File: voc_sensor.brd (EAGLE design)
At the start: 28 x 32 mm, 14 parts, among them IC1 MP901, IC2 DS2438, IC3 7805DT, X1 MSTBV3

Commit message: changing some values: 5 Ohm resistor to 5.1 Ohm (5 Ohm is not broadly available) selected different type of TVS diode with essentially the same ratings
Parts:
- D1, D8: value SMA6F7.5A -> SMAJ7.5A-LF
- R1, R2, R4: value 5 -> 5.1
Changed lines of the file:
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@@
 <attribute name="NAME" x="15.105" y="1.867" size="1.016" layer="26" rot="MR0"/>
 </element>
-<element name="R1" library="rcl" package="R0402" value="5" x="8.6" y="6.8" smashed="yes" rot="MR180">
+<element name="R1" library="rcl" package="R0402" value="5.1" x="8.6" y="6.8" smashed="yes" rot="MR180">
 <attribute name="NAME" x="7.565" y="5.965" size="1.016" layer="26" rot="MR180"/>
 <attribute name="VALUE" x="7.965" y="8.705" size="1.016" layer="28" rot="MR180"/>
 </element>
-<element name="R2" library="rcl" package="R0402" value="5" x="6" y="25.4" smashed="yes" rot="MR180">
+<element name="R2" library="rcl" package="R0402" value="5.1" x="6" y="25.4" smashed="yes" rot="MR180">
 <attribute name="NAME" x="5.365" y="24.765" size="1.016" layer="26" rot="MR180"/>
 <attribute name="VALUE" x="5.365" y="27.105" size="1.016" layer="28" rot="MR180"/>
 </element>
-<element name="D8" library="diodes" package="DO214AC" value="SMA6F7.5A" x="3.8" y="6.8" smashed="yes" rot="MR0">
+<element name="D8" library="diodes" package="DO214AC" value="SMAJ7.5A-LF" x="3.8" y="6.8" smashed="yes" rot="MR0">
 <attribute name="NAME" x="4.64" y="3.886" size="1.016" layer="26" ratio="10" rot="MR0"/>
 </element>
@@
 <element name="IC3" library="linear" package="TO252" value="7805DT" x="20.4" y="25.8" smashed="yes" rot="MR270">
 <attribute name="NAME" x="25.59" y="27.14" size="1.016" layer="26" rot="MR270"/>
+<attribute name="MANF#" value="MC7805BDTG" x="20.4" y="25.8" size="1.778" layer="28" rot="MR270" display="off"/>
 </element>
 <element name="C1" library="rcl" package="C0805K" value="100n" x="12.6" y="28.6" smashed="yes" rot="MR270">
@@
 <attribute name="VALUE" x="9.9" y="31.8" size="1.016" layer="28" rot="MR270"/>
 </element>
-<element name="D1" library="diodes" package="DO214AC" value="SMA6F7.5A" x="2.4" y="27.4" smashed="yes" rot="MR270">
+<element name="D1" library="diodes" package="DO214AC" value="SMAJ7.5A-LF" x="2.4" y="27.4" smashed="yes" rot="MR270">
 <attribute name="NAME" x="1.114" y="28.24" size="1.016" layer="26" ratio="10" rot="MR270"/>
 </element>
-<element name="R4" library="rcl" package="R0402" value="5" x="5.8" y="29.4" smashed="yes" rot="MR180">
+<element name="R4" library="rcl" package="R0402" value="5.1" x="5.8" y="29.4" smashed="yes" rot="MR180">
 <attribute name="NAME" x="5.165" y="28.765" size="1.016" layer="26" rot="MR180"/>
 <attribute name="VALUE" x="5.365" y="31.105" size="1.016" layer="28" rot="MR180"/>

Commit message: changing load resistor to 100k as stated on the sensor packaging... already tried this and it works like a charm
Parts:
- R3: value 17k -> 100k
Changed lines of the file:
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@@
 <attribute name="NAME" x="1.496" y="14.945" size="1.016" layer="25" ratio="10" rot="R90"/>
 </element>
-<element name="R3" library="rcl" package="R0402" value="17k" x="15" y="10" smashed="yes" rot="MR0">
+<element name="R3" library="rcl" package="R0402" value="100k" x="15" y="10" smashed="yes" rot="MR0">
 <attribute name="NAME" x="19.035" y="9.435" size="1.016" layer="26" rot="MR0"/>
 <attribute name="VALUE" x="13.635" y="9.495" size="1.016" layer="28" rot="MR0"/>

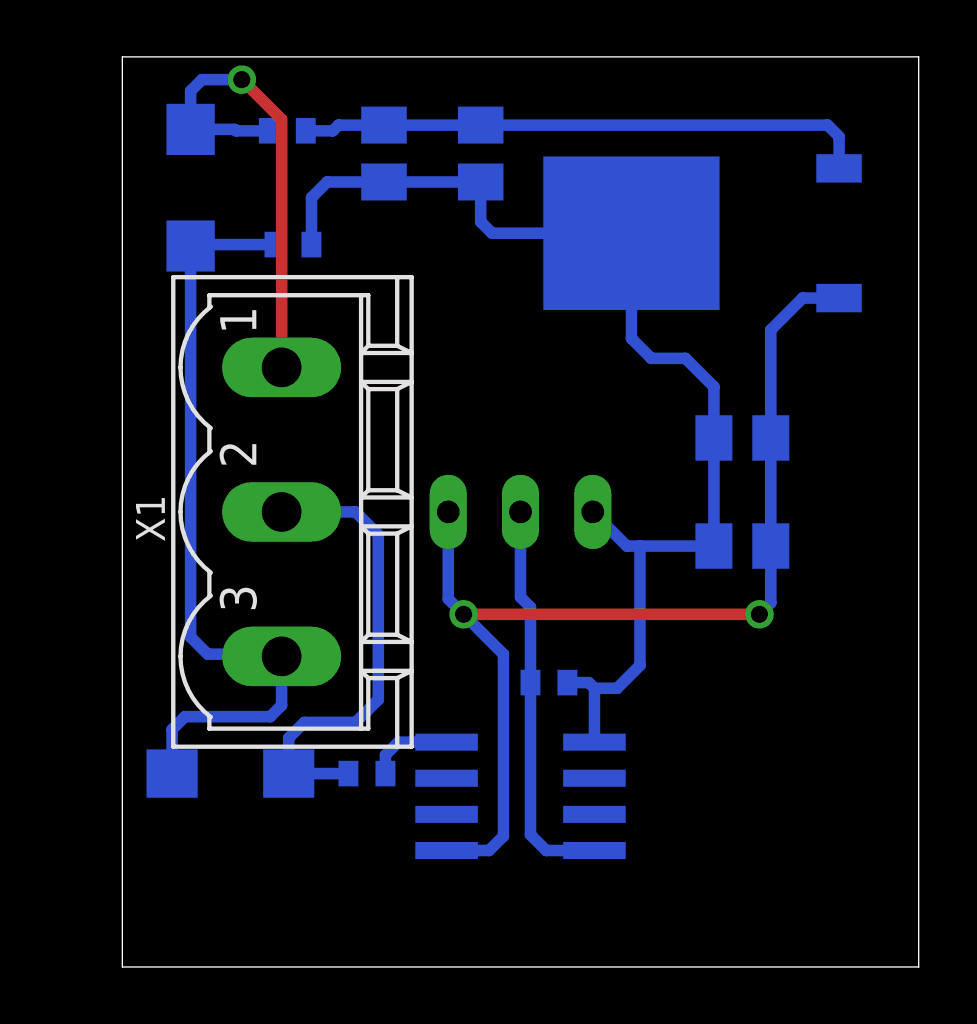
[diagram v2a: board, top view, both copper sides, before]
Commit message: replaced connector X1 to get a lower profile inside of the wall insert (resolves issue #2)
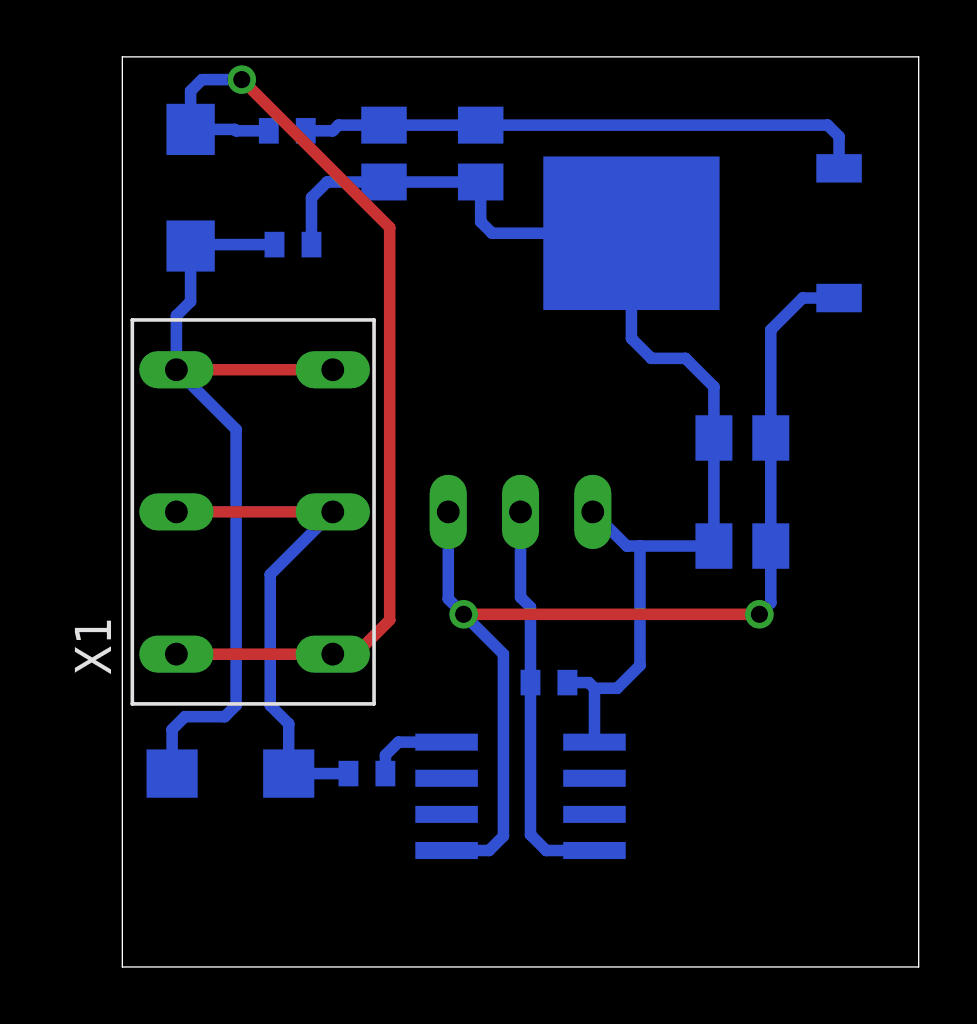
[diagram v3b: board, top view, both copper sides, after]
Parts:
- X1: value MSTBV3 -> SPRING_CLAMP_3_AST215; device con-phoenix-508:MSTBV3 -> connectors:AST215_3
- moved X1 1.00 mm to (4.60, 16.0), turned to 90 degrees
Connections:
- net N$10: now also X1.2A, X1.2B; no longer X1.2
- net N$4: now also X1.1A, X1.1B; no longer X1.1
- net N$5: now also X1.3A, X1.3B; no longer X1.3
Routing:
- net N$4: track 16.8 -> 35.2 mm
- net N$5: track 27.7 -> 29.8 mm
- net N$10: track 16.6 -> 18.0 mm
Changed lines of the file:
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@@
 <attribute name="NAME" x="4.64" y="3.886" size="1.016" layer="26" ratio="10" rot="MR0"/>
-</element>
-<element name="X1" library="con-phoenix-508" package="MSTBV3" value="MSTBV3" x="5.6" y="16" smashed="yes" rot="R270">
-<attribute name="OC_NEWARK" value="69R9846" x="-11.4" y="16" size="1.778" layer="27" rot="R270" display="off"/>
-<attribute name="MPN" value="MSTBV 2,5/3-GF-5.08" x="-11.4" y="16" size="1.778" layer="27" rot="R270" display="off"/>
-<attribute name="MF" value="" x="-11.4" y="16" size="1.778" layer="27" rot="R270" display="off"/>
-<attribute name="OC_FARNELL" value="1792793" x="-11.4" y="16" size="1.778" layer="27" rot="R270" display="off"/>
-<attribute name="NAME" x="1.496" y="14.945" size="1.016" layer="25" ratio="10" rot="R90"/>
 </element>
 <element name="R3" library="rcl" package="R0402" value="100k" x="15" y="10" smashed="yes" rot="MR0">
@@
 <attribute name="VALUE" x="5.365" y="31.105" size="1.016" layer="28" rot="MR180"/>
 </element>
+<element name="X1" library="connectors" package="AST215_3" value="SPRING_CLAMP_3_AST215" x="4.6" y="16" rot="R90"/>
 </elements>
 <signals>
@@
 <contactref element="R1" pad="1"/>
 <contactref element="D8" pad="C"/>
-<contactref element="X1" pad="2"/>
 <wire x1="5.85" y1="6.8" x2="7.95" y2="6.8" width="0.4064" layer="16"/>
-<wire x1="5.85" y1="6.8" x2="5.85" y2="8.05" width="0.4064" layer="16"/>
-<wire x1="5.85" y1="8.05" x2="6.4" y2="8.6" width="0.4064" layer="16"/>
-<wire x1="6.4" y1="8.6" x2="8.2" y2="8.6" width="0.4064" layer="16"/>
-<wire x1="8.2" y1="8.6" x2="9" y2="9.4" width="0.4064" layer="16"/>
-<wire x1="9" y1="9.4" x2="9" y2="15.2" width="0.4064" layer="16"/>
-<wire x1="9" y1="15.2" x2="8.2" y2="16" width="0.4064" layer="16"/>
-<wire x1="8.2" y1="16" x2="5.6" y2="16" width="0.4064" layer="16"/>
+<contactref element="X1" pad="2A"/>
+<contactref element="X1" pad="2B"/>
+<wire x1="7.4" y1="16" x2="1.9" y2="16" width="0.4064" layer="1"/>
+<wire x1="7.4" y1="16" x2="5.2" y2="13.8" width="0.4064" layer="16"/>
+<wire x1="5.2" y1="13.8" x2="5.2" y2="9.2" width="0.4064" layer="16"/>
+<wire x1="5.2" y1="9.2" x2="5.85" y2="8.55" width="0.4064" layer="16"/>
+<wire x1="5.85" y1="8.55" x2="5.85" y2="6.8" width="0.4064" layer="16"/>
 </signal>
 <signal name="N$20">
@@
 </signal>
 <signal name="N$4">
-<contactref element="X1" pad="1"/>
 <contactref element="R4" pad="1"/>
 <contactref element="D1" pad="C"/>
-<wire x1="5.6" y1="21.08" x2="5.6" y2="29.8" width="0.4064" layer="1"/>
-<wire x1="5.6" y1="29.8" x2="4.2" y2="31.2" width="0.4064" layer="1"/>
 <via x="4.2" y="31.2" extent="1-16" drill="0.6"/>
 <wire x1="4.2" y1="31.2" x2="2.8" y2="31.2" width="0.4064" layer="16"/>
@@
 <wire x1="4" y1="29.4" x2="3.95" y2="29.45" width="0.4064" layer="16"/>
 <wire x1="3.95" y1="29.45" x2="2.4" y2="29.45" width="0.4064" layer="16"/>
+<contactref element="X1" pad="1A"/>
+<contactref element="X1" pad="1B"/>
+<wire x1="7.4" y1="11" x2="1.9" y2="11" width="0.4064" layer="1"/>
+<wire x1="4.2" y1="31.2" x2="9.4" y2="26" width="0.4064" layer="1"/>
+<wire x1="9.4" y1="26" x2="9.4" y2="12.2" width="0.4064" layer="1"/>
+<wire x1="9.4" y1="12.2" x2="8.2" y2="11" width="0.4064" layer="1"/>
+<wire x1="8.2" y1="11" x2="7.4" y2="11" width="0.4064" layer="1"/>
 </signal>
 <signal name="N$2">
@@
 <contactref element="R2" pad="1"/>
 <contactref element="D8" pad="A"/>
-<contactref element="X1" pad="3"/>
 <contactref element="D1" pad="A"/>
 <wire x1="2.2" y1="8.8" x2="1.75" y2="8.35" width="0.4064" layer="16"/>
 <wire x1="1.75" y1="8.35" x2="1.75" y2="6.8" width="0.4064" layer="16"/>
-<wire x1="2.2" y1="8.8" x2="5.2" y2="8.8" width="0.4064" layer="16"/>
-<wire x1="5.2" y1="8.8" x2="5.6" y2="9.2" width="0.4064" layer="16"/>
-<wire x1="5.6" y1="9.2" x2="5.6" y2="10.92" width="0.4064" layer="16"/>
-<wire x1="2.4" y1="25.35" x2="2.4" y2="11.6" width="0.4064" layer="16"/>
-<wire x1="2.4" y1="11.6" x2="3" y2="11" width="0.4064" layer="16"/>
-<wire x1="3" y1="11" x2="5.52" y2="11" width="0.4064" layer="16"/>
-<wire x1="5.52" y1="11" x2="5.6" y2="10.92" width="0.4064" layer="16"/>
+<wire x1="2.2" y1="8.8" x2="5.2" y2="8.8" width="0" layer="19" extent="1-16"/>
 <wire x1="2.4" y1="25.35" x2="2.45" y2="25.4" width="0.4064" layer="16"/>
 <wire x1="2.45" y1="25.4" x2="5.35" y2="25.4" width="0.4064" layer="16"/>
+<contactref element="X1" pad="3A"/>
+<contactref element="X1" pad="3B"/>
+<wire x1="7.4" y1="21" x2="1.9" y2="21" width="0.4064" layer="1"/>
+<wire x1="2.2" y1="8.8" x2="3.6" y2="8.8" width="0.4064" layer="16"/>
+<wire x1="3.6" y1="8.8" x2="4" y2="9.2" width="0.4064" layer="16"/>
+<wire x1="4" y1="9.2" x2="4" y2="18.9" width="0.4064" layer="16"/>
+<wire x1="4" y1="18.9" x2="1.9" y2="21" width="0.4064" layer="16"/>
+<wire x1="2.4" y1="25.35" x2="2.4" y2="23.4" width="0.4064" layer="16"/>
+<wire x1="2.4" y1="23.4" x2="1.9" y2="22.9" width="0.4064" layer="16"/>
+<wire x1="1.9" y1="22.9" x2="1.9" y2="21" width="0.4064" layer="16"/>
 </signal>
 </signals>

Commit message: changing the 5V regulator to a switching type and adding some stuff to make the revision visible on the board without guesswork
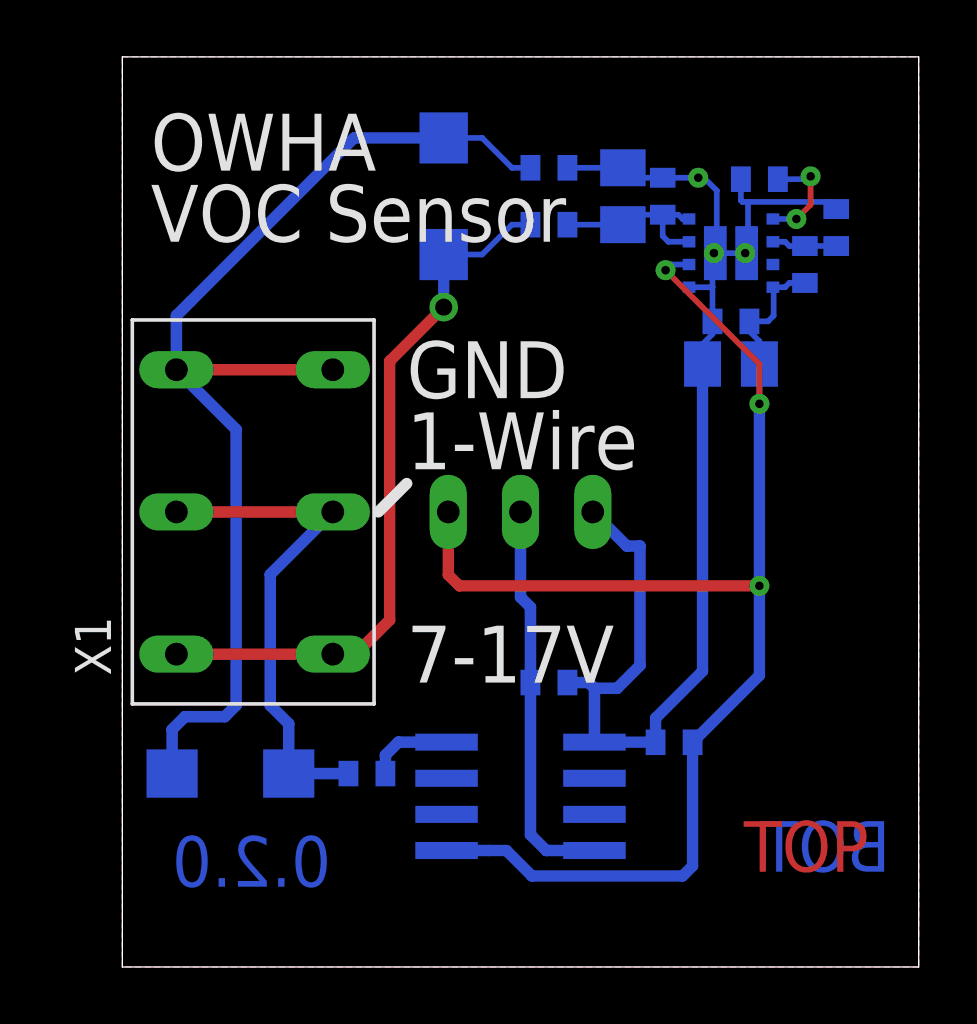
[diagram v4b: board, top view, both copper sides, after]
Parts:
- removed IC3: 7805DT, linear:TO252
- added C5: 3300p, rcl:C0402
- added C6: 100n, rcl:C0402
- added IC4: LMZ21700, ic_voltage_regulator:LMZ21700
- added R5: 232k, rcl:R0402
- added R6: 44.2k, rcl:R0402
- C1, C3: device rcl:C0805K -> rcl:C0402
- C2, C4: value 1µ -> 22µ
- moved R4 9.77 mm to (15.0, 26.1)
- moved R2 9.40 mm to (15.0, 28.1)
- moved D1 8.91 mm to (11.3, 27.1), turned to 90 degrees
- moved C4 8.53 mm to (17.6, 27.1), turned to 90 degrees
- moved C1 6.57 mm to (19.0, 27.1), turned to 90 degrees
- moved C2 6.41 mm to (21.4, 21.2)
- moved C3 4.12 mm to (21.4, 22.7)
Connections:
- removed net N$2: C2.1, C3.1, IC1.1, IC2.5, IC3.2
- new net N$6: C5.1, IC4.1
- new net N$7: IC4.2, R5.1, R6.2
- new net VCC: C2.1, C3.1, C6.1, IC1.1, IC2.5, IC4.4, IC4.6, R5.2
- net GND: now also C5.2, C6.2, IC4.5, IC4.TPAD@1, IC4.TPAD@2, R6.1; no longer IC3.3
- net N$3: now also IC4.7, IC4.8; no longer IC3.1
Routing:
- net VCC: track 0.00 -> 52.9 mm, vias 0 -> 3
- net N$2: track 37.8 -> 0.00 mm, vias 2 -> 0
- net N$3: track 20.1 -> 6.24 mm
- net N$4: track 35.2 -> 25.1 mm
- net N$5: track 29.8 -> 39.7 mm
- net GND: track 41.4 -> 47.2 mm, vias 0 -> 3
- net N$6: track 0.00 -> 3.72 mm, vias 0 -> 2
- net N$7: track 0.00 -> 2.29 mm
- added copper zone on layer 1, net GND
- added copper zone on layer 16, net GND
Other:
- board text added: "1-Wire"
- board text added: "7-17V"
- board text added: ">DRAWING_NAME"
- board text added: ">REVISION"
- board text added: "BOT"
- board text added: "GND"
- board text added: "OWHA"
- board text added: "TOP"
- board text added: "VOC Sensor"

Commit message: moving clamping terminal to get out of the way of case parts and removing some DRC errors
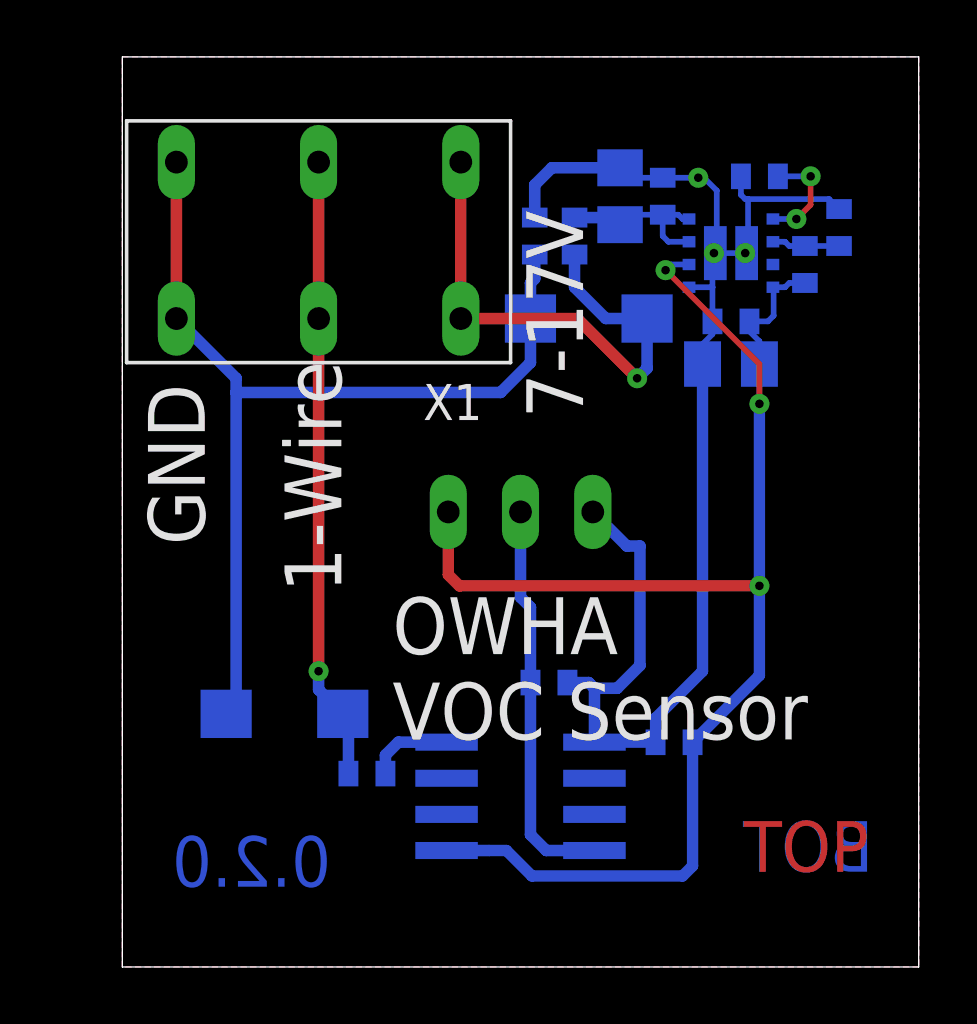
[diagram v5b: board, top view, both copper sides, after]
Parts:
- moved X1 9.77 mm to (6.90, 25.5), turned to 180 degrees
- moved D1 6.67 mm to (16.4, 22.8), turned to 0 degrees
- moved D8 2.83 mm to (5.70, 8.90)
- moved R2 2.45 mm to (14.5, 25.7), turned to 90 degrees
- moved R4 0.98 mm to (15.9, 25.7), turned to 90 degrees
- moved C4 0.10 mm to (17.5, 27.1)
- moved C5 0.10 mm to (22.4, 27.8)
- moved R6 0.10 mm to (25.2, 26.0)
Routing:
- net N$4: track 25.1 -> 19.0 mm
- net N$5: track 39.7 -> 35.2 mm
- net N$10: track 18.0 -> 21.9 mm, vias 0 -> 1
- net GND: track 47.2 -> 50.0 mm
